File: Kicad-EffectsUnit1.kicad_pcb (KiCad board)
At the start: 2 copper layers, 100 x 100 mm, 167 parts, among them J101 In7, J102 Doepfer connector, J103 Vin 7-12v, J104 In6, J105 In3, J106 Out10, J107 Out11, J108 Out12, J109 Out13, J110 Power Conn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

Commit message: 3D + PCB
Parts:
- removed REF**: Gauge_100mm_Grid_Type1_Silk_CopperTop, AJ:Gauge_100mm_Grid_Type1_Silk_CopperTop
- removed SW103: Rotary_Encoder_Switch, Rotary_Encoder:RotaryEncoder_Alps_EC11E-Switch_Vertical_H20mm
- added C118: 100n, Capacitor_SMD:C_0805_2012Metric_Pad1.15x1.40mm_HandSolder, F.Cu at (57.9, 101.3)
- added C121: 100n, Capacitor_SMD:C_0805_2012Metric_Pad1.15x1.40mm_HandSolder, F.Cu at (61.6, 101.3)
- added RV104: 10k_A4, Potentiometer_THT:Potentiometer_China_RK09_Single_Vertical_AJ, F.Cu at (102.5, 126.5)
- added RV105: 10k_A5, Potentiometer_THT:Potentiometer_China_RK09_Single_Vertical_AJ, F.Cu at (102.5, 114.0)
- added SW105: Dist 10, AJ-Dropbox-Kicad:SPDTx2, F.Cu at (110.0, 66.5)
- D103, D104, D105, D107, D109, D112, D118: moved to F.Cu
- D113: value LED_Out12 -> LED_Out6; moved to F.Cu
- D114: value LED_Out13 -> LED_Out9; moved to F.Cu
- J108: value Out12 -> Out9
- J109: value Out13 -> Out6
- RV101: value 10k_O10 -> 10k_O6
- RV103: value 100k_O12 -> 100k_O10
- SW101: value Dist 10 -> Dist 6
- SW102: value Crush A3 -> Crush A6
- SW104: value Dist 12 -> Rotary_Encoder_Switch; footprint AJ-Dropbox-Kicad:SPDTx2 -> Rotary_Encoder:RotaryEncoder_Alps_EC11E-Switch_Vertical_H20mm
- moved D109 116.5 mm to (90.9, 139.2)
- moved D112 103.7 mm to (91.8, 130.9)
- moved J101 100.0 mm to (130.0, 135.0), turned to 90 degrees
- moved D103 99.2 mm to (79.5, 130.5)
- moved RV102 93.0 mm to (137.5, 121.5), turned to 180 degrees
- moved D118 83.9 mm to (84.5, 101.0)
- moved D104 78.7 mm to (76.5, 117.0)
- moved D107 75.1 mm to (82.4, 122.7)
- moved J107 74.5 mm to (130.0, 111.5), turned to 90 degrees
- moved J102 74.0 mm to (119.0, 52.0)
- moved J110 72.2 mm to (97.0, 55.0)
- moved A101 67.4 mm to (73.0, 3.00)
- moved RV103 63.3 mm to (102.5, 82.5), turned to 0 degrees
- moved J104 62.2 mm to (130.0, 100.5), turned to 90 degrees
- moved RV101 55.3 mm to (137.5, 77.5), turned to 180 degrees
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- renumbered C118 to C119, C119 to C120, C120 to C122, C121 to C123
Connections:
- A101 pad 10: LED-Out11 -> LED-Out6
- A101 pad 11: LED-Out12 -> LED-Out9
- A101 pad 12: LED-Out13 -> Out9
- A101 pad 15: Out12 -> LED-Out10
- A101 pad 16: Out13 -> LED-Out11
- A101 pad 23: (no net) -> SDA-A4
- A101 pad 24: (no net) -> SCL-A5
- A101 pad 9: LED-Out10 -> Out6
- C122 pad 1: Out13Dist -> Out9Dist
- D110 pad 2: Out10Dist -> Out6Dist
- D111 pad 1: Out10Dist -> Out6Dist
- J108 pad T: Out12Dist -> Out9Dist
- J109 pad T: Out13Dist -> Out6Dist
- R115 pad 1: Out10Dist -> Out6Dist
- R118 pad 1: LED-Out12 -> LED-Out6
- R121 pad 1: LED-Out13 -> LED-Out9
- R124 pad 2: A6 -> A7
- R129 pad 1: Out12Dist -> Out10Dist
- R130 pad 1: Out12Dist -> Out10Dist
- R131 pad 2: Out12 -> Out10
- R133 pad 2: A7 -> A3
- R136 pad 1: Out13Dist -> Out9Dist
- R137 pad 1: Out13Dist -> Out9Dist
- R138 pad 2: Out13 -> Out9
- SW102 pad 1: Out10 -> Out6
- SW102 pad 3: A3 -> A6

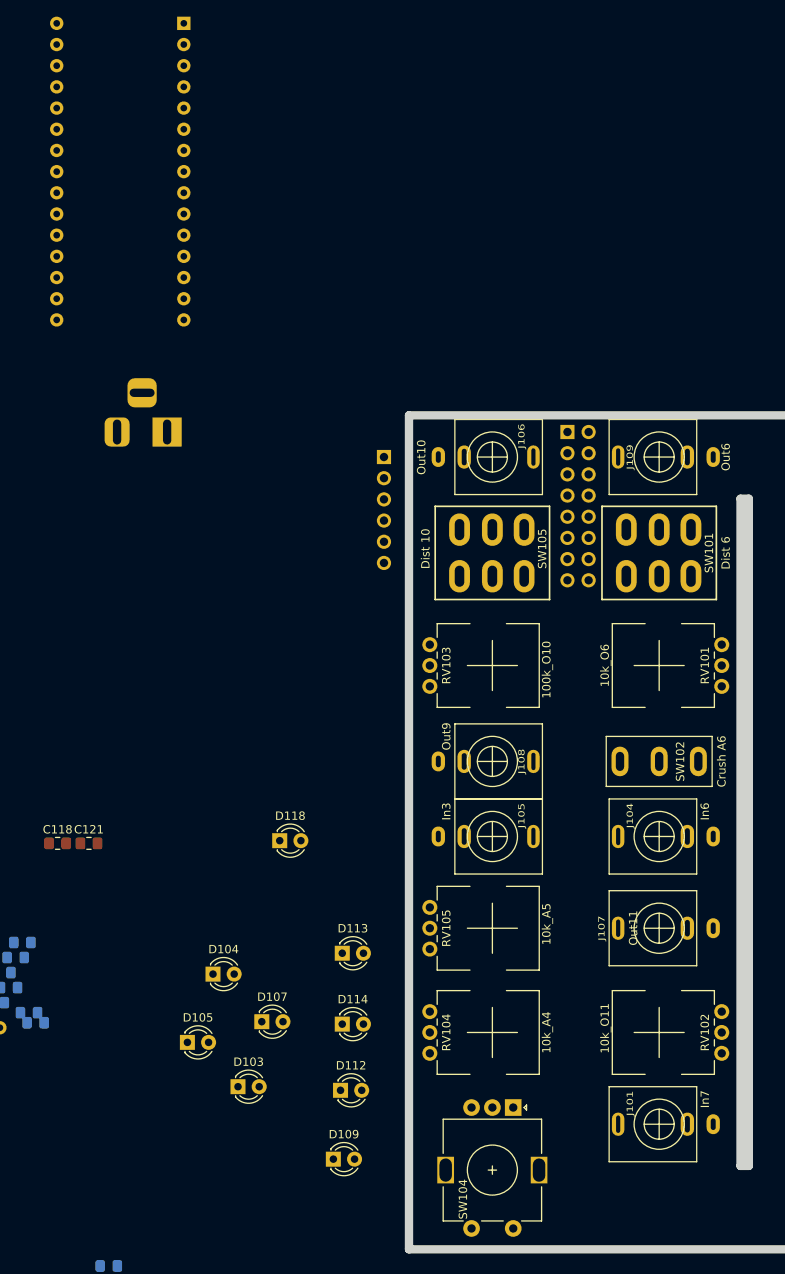
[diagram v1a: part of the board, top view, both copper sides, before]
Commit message: Removed components from PSU
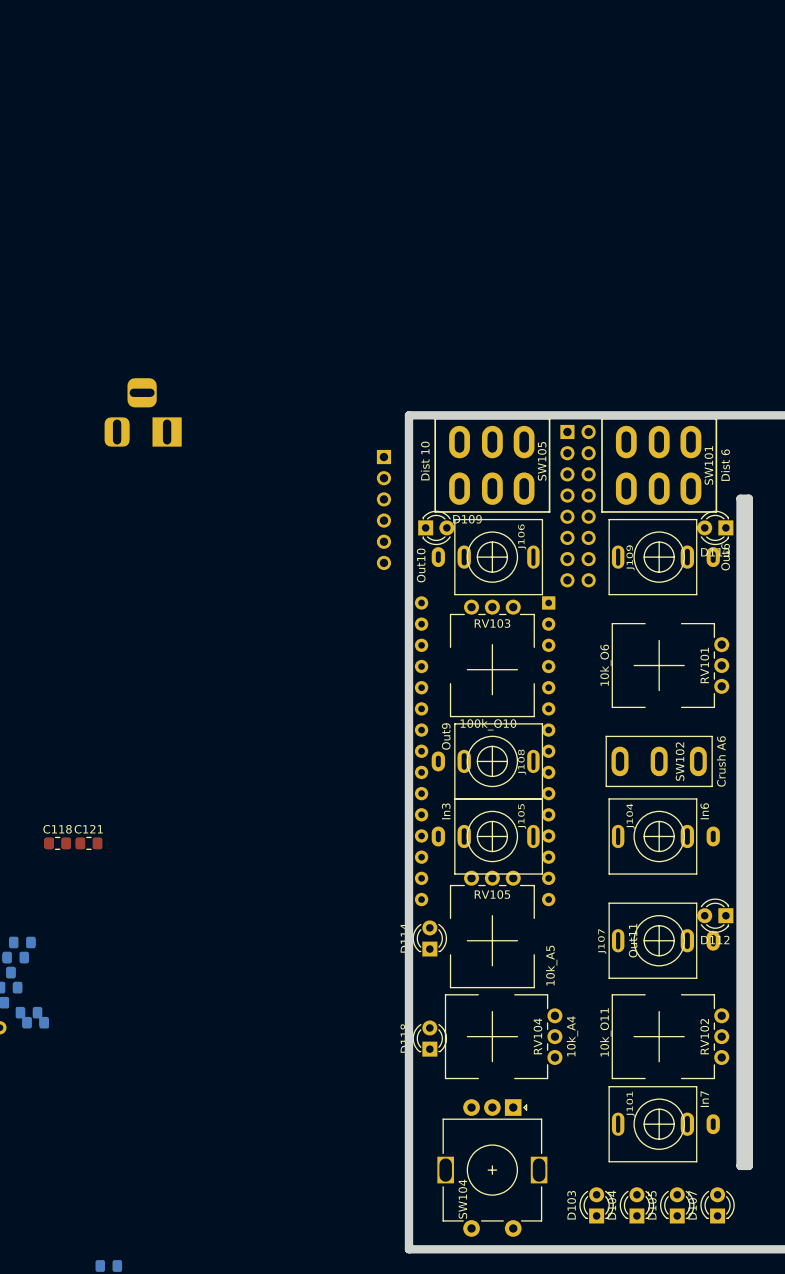
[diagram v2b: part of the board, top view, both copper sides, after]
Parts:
- moved A101 82.1 mm to (116.8, 72.5)
- moved D109 76.5 mm to (102.0, 63.5)
- moved D113 68.7 mm to (138.0, 63.5), turned to 180 degrees
- moved D105 62.3 mm to (132.2, 146.0), turned to 90 degrees
- moved D107 59.4 mm to (137.0, 146.0), turned to 90 degrees
- moved D104 58.5 mm to (127.3, 146.0), turned to 90 degrees
- moved D112 50.7 mm to (138.0, 110.0), turned to 180 degrees
- moved D103 45.7 mm to (122.5, 146.0), turned to 90 degrees
- moved D118 30.8 mm to (102.5, 126.0), turned to 90 degrees
- moved RV104 15.7 mm to (117.5, 122.0), turned to 180 degrees
- moved D114 13.8 mm to (102.5, 114.0), turned to 90 degrees
- moved J106 12.0 mm to (110.0, 67.0)
- moved J109 12.0 mm to (130.0, 67.0)
- moved RV103 10.7 mm to (107.5, 73.0), turned to 270 degrees
- moved SW101 10.5 mm to (130.0, 56.0)
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
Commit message: misc
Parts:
- removed C101: 100uF, Capacitor_THT:CP_Radial_D5.0mm_P2.50mm
- removed C102, C103: 100n, Capacitor_SMD:C_0805_2012Metric_Pad1.15x1.40mm_HandSolder
- removed F102: Polyfuse, Fuse:Fuse_1206_3216Metric_Pad1.42x1.75mm_HandSolder
- removed J103: Vin 7-12v, Connector_BarrelJack:BarrelJack_Horizontal
- removed J110: Power Conn, Connector_PinHeader_2.54mm:PinHeader_1x06_P2.54mm_Vertical
- removed R102: 10M, Resistor_SMD:R_0805_2012Metric_Pad1.15x1.40mm_HandSolder
- C118, C121: moved to B.Cu
- D110, D111: footprint Diode_SMD:D_SOD-123 -> Diode_SMD:D_0805_2012Metric_Pad1.15x1.40mm_HandSolder
- D117: value LED_Out11 -> LED_11dist
- D118: value LED_CV2 -> LED_11dist; footprint LED_THT:LED_D3.0mm -> Diode_SMD:D_0805_2012Metric_Pad1.15x1.40mm_HandSolder; moved to B.Cu
- moved F101 124.6 mm to (116.5, 57.0), turned to 270 degrees
- moved C106 116.9 mm to (128.0, 67.5), turned to 270 degrees
- moved C105 92.4 mm to (110.0, 63.5), turned to 180 degrees
- moved C110 85.4 mm to (113.0, 67.5), turned to 270 degrees
- moved C118 66.8 mm to (119.5, 127.0), turned to 270 degrees
- moved C119 53.0 mm to (86.8, 73.1)
- moved R114 53.0 mm to (74.8, 68.9)
- moved R125 53.0 mm to (68.4, 59.8)
- moved C107 53.0 mm to (56.5, 56.8)
- moved C108 53.0 mm to (54.9, 58.0)
- moved C109 53.0 mm to (57.3, 83.9)
- moved C111 53.0 mm to (54.1, 61.0)
- moved C112 53.0 mm to (53.3, 59.2)
- moved C123 53.0 mm to (76.4, 66.5)
- moved D101 53.0 mm to (62.9, 61.6)
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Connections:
- A101 pad 17: Net-(A101-Pad17) -> (no net)
- A101 pad 30: VCC -> (no net)
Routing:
- net +12V: track 0.00 -> 52.5 mm
- net -12V: track 0.00 -> 43.9 mm
- net +5V: track 0.00 -> 29.2 mm
- net GND: track 0.00 -> 7.62 mm
- net /+5Vin: track 0.00 -> 5.68 mm
- net /Gate: track 0.00 -> 2.54 mm
- net /CV: track 0.00 -> 2.54 mm

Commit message: PREPARE for major restruct
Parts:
- removed C109, C113: 100n, Capacitor_SMD:C_0805_2012Metric_Pad1.15x1.40mm_HandSolder
- moved R127 88.3 mm to (108.2, 145.8), turned to 180 degrees
- moved R122 83.7 mm to (129.0, 116.5), turned to 270 degrees
- moved C108 81.1 mm to (130.0, 88.8), turned to 180 degrees
- moved D117 78.6 mm to (127.0, 116.5), turned to 90 degrees
- moved R112 76.7 mm to (146.0, 82.0)
- moved U101 74.6 mm to (123.5, 86.2)
- moved D122 70.1 mm to (94.0, 47.2)
- moved C111 69.3 mm to (120.2, 81.8), turned to 180 degrees
- moved D116 64.7 mm to (122.0, 79.8), turned to 180 degrees
- moved C112 60.9 mm to (110.0, 81.5)
- moved D101 60.6 mm to (123.5, 62.8), turned to 270 degrees
- moved D121 60.5 mm to (94.0, 51.8)
- moved C107 59.1 mm to (111.0, 79.5), turned to 180 degrees
- moved U102 53.6 mm to (110.0, 86.2)
- moved R125 52.3 mm to (104.5, 97.8), turned to 180 degrees
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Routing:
- net +5V: track 29.2 -> 83.2 mm
- net GND: track 7.62 -> 37.6 mm
- net SCL-A5: track 0.00 -> 27.7 mm, vias 0 -> 1
- net +12V: track 52.5 -> 74.0 mm, vias 0 -> 2
- net Net-(SW102-Pad2): track 0.00 -> 19.6 mm
- net A3: track 0.00 -> 14.3 mm, vias 0 -> 1
- net Net-(D106-Pad1): track 0.00 -> 8.01 mm
- net Out11Dist: track 0.00 -> 5.78 mm
- net Btn: track 0.00 -> 5.37 mm
- net A1: track 0.00 -> 2.03 mm
- net A2: track 0.00 -> 2.01 mm
- net -12V: track 43.9 -> 45.2 mm

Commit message: Reorganize #1
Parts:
- moved R124 80.1 mm to (124.7, 104.2), turned to 90 degrees
- moved C117 77.5 mm to (113.8, 62.2), turned to 180 degrees
- moved R104 73.3 mm to (125.2, 96.0), turned to 90 degrees
- moved R119 59.2 mm to (131.5, 32.2)
- moved R121 56.4 mm to (118.5, 104.5), turned to 180 degrees
- moved R132 52.1 mm to (114.8, 108.0)
- moved R111 50.7 mm to (130.0, 36.2)
- moved C108 39.9 mm to (90.2, 85.8)
- moved D108 37.1 mm to (133.8, 43.2)
- moved D116 37.1 mm to (126.8, 43.0)
- moved R131 35.2 mm to (118.5, 108.0)
- moved R134 31.3 mm to (103.5, 52.2), turned to 90 degrees
- moved U101 22.9 mm to (130.0, 108.2)
- moved C111 22.9 mm to (98.3, 75.2)
- moved C107 19.8 mm to (91.3, 77.8)
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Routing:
- net Net-(C117-Pad2): track 0.00 -> 60.8 mm
- net +5V: track 83.2 -> 37.9 mm
- net -12V: track 45.2 -> 78.1 mm
- net +12V: track 74.0 -> 103.2 mm, vias 2 -> 0
- net SCL-A5: track 27.7 -> 0.67 mm, vias 1 -> 0
- net Out10Dist: track 0.00 -> 26.0 mm
- net Net-(SW102-Pad2): track 19.6 -> 0.00 mm
- net GND: track 37.6 -> 19.4 mm
- net Net-(R134-Pad2): track 0.00 -> 11.8 mm
- net Net-(D106-Pad1): track 8.01 -> 0.00 mm
- net Net-(D121-Pad1): track 0.00 -> 6.57 mm
- net Net-(D119-Pad2): track 0.00 -> 6.48 mm
- net A3: track 14.3 -> 8.20 mm, vias 1 -> 0
- net Btn: track 5.37 -> 0.00 mm
- net Net-(C117-Pad1): track 0.00 -> 3.86 mm
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
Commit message: Distortion - Bitcrunch components placed
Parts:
- moved R113 101.8 mm to (136.0, 141.0)
- moved H102 97.2 mm to (169.0, 159.9)
- moved H101 97.2 mm to (169.8, 155.7)
- moved R130 91.6 mm to (109.6, 70.4), turned to 270 degrees
- moved R119 85.3 mm to (133.2, 117.5), turned to 270 degrees
- moved R117 84.8 mm to (138.0, 60.2), turned to 90 degrees
- moved H103 83.6 mm to (160.0, 137.6)
- moved D111 82.4 mm to (130.0, 69.2), turned to 90 degrees
- moved R120 81.3 mm to (137.5, 120.0), turned to 90 degrees
- moved D106 80.8 mm to (130.2, 62.2)
- moved D116 74.5 mm to (135.2, 117.0), turned to 270 degrees
- moved R110 74.5 mm to (131.0, 141.0)
- moved R115 73.3 mm to (133.0, 71.0)
- moved R118 72.0 mm to (133.0, 73.0)
- moved R137 69.8 mm to (109.8, 91.6)
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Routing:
- net A7: track 0.00 -> 108.9 mm
- net Net-(D106-Pad1): track 0.00 -> 90.0 mm
- net Net-(R115-Pad2): track 0.00 -> 66.8 mm, vias 0 -> 2
- net GND: track 19.4 -> 82.3 mm, vias 0 -> 1
- net Btn: track 0.00 -> 48.2 mm, vias 0 -> 3
- net SDA-A4: track 0.00 -> 42.0 mm
- net A2: track 0.00 -> 39.0 mm, vias 0 -> 3
- net A1: track 0.00 -> 37.0 mm, vias 0 -> 3
- net Net-(R130-Pad2): track 0.00 -> 31.7 mm, vias 0 -> 2
- net SCL-A5: track 0.67 -> 32.1 mm, vias 0 -> 2
- net Net-(R137-Pad2): track 0.00 -> 24.0 mm
- net Out6: track 0.00 -> 22.3 mm, vias 0 -> 2
- net Net-(RV103-Pad2): track 0.00 -> 21.2 mm
- net Out9Dist: track 0.00 -> 20.3 mm, vias 0 -> 4
- net Net-(D110-Pad1): track 0.00 -> 20.1 mm
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
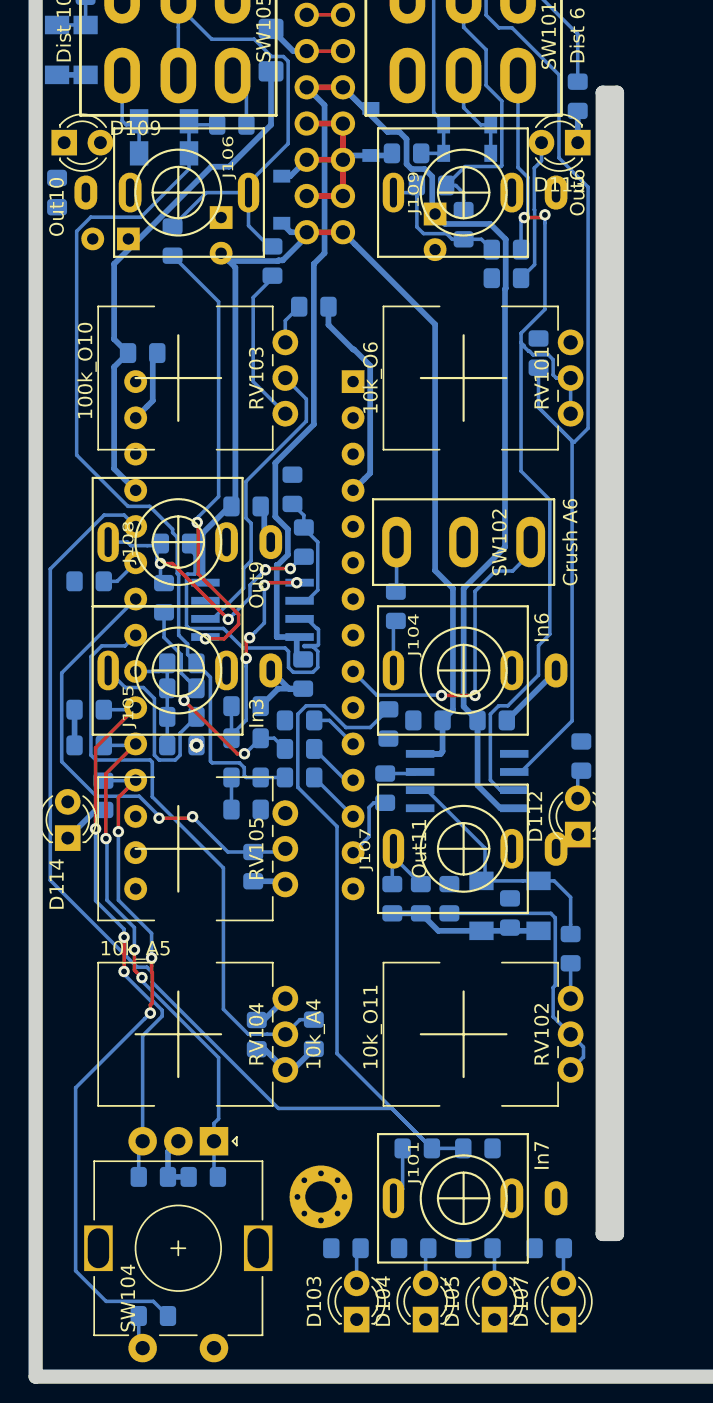
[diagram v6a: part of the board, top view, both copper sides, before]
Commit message: Before gnd flooding
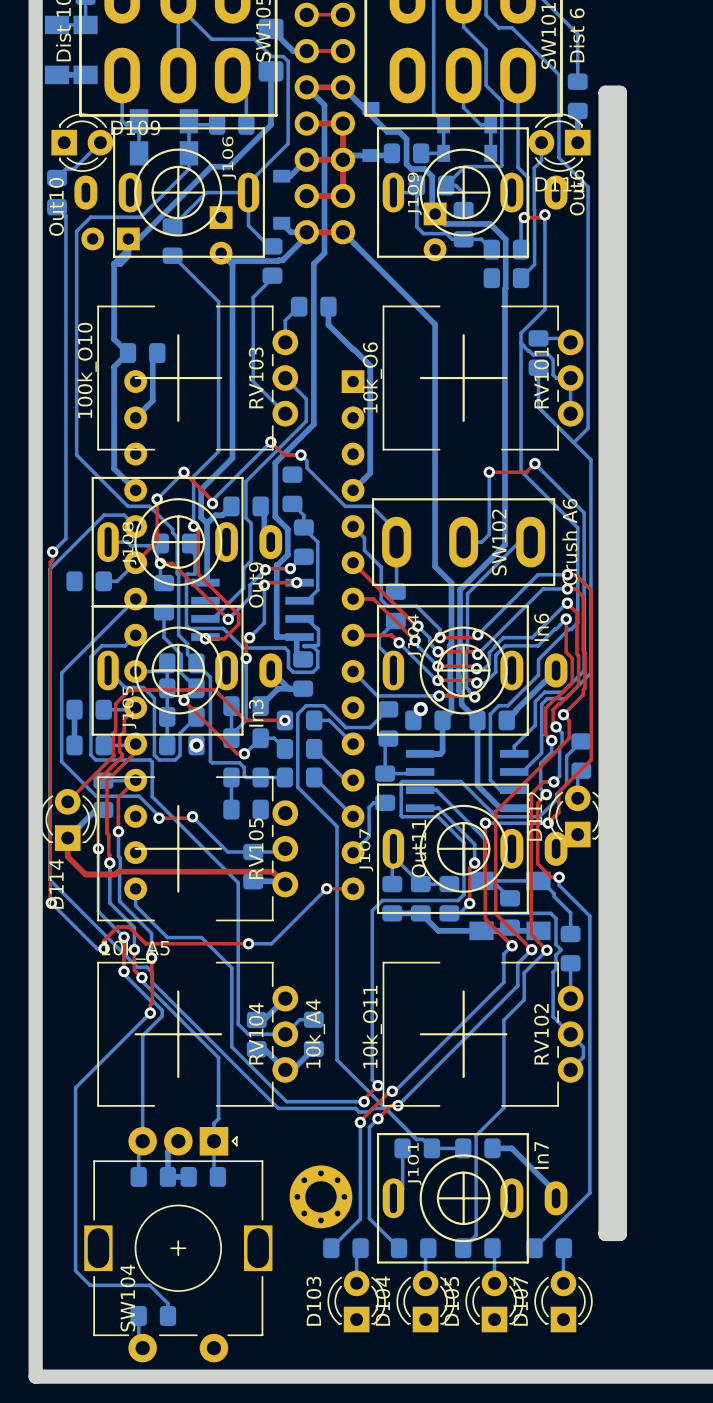
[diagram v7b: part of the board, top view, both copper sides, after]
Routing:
- net LED1: track 0.00 -> 82.4 mm, vias 0 -> 8
- net LED2: track 0.00 -> 76.7 mm, vias 0 -> 8
- net LED-Out11: track 0.00 -> 75.4 mm, vias 0 -> 2
- net LED-Out10: track 0.00 -> 75.1 mm, vias 0 -> 5
- net LED3: track 0.00 -> 70.3 mm, vias 0 -> 7
- net LED4: track 0.00 -> 68.3 mm, vias 0 -> 7
- net Net-(SW102-Pad2): track 0.00 -> 34.4 mm, vias 0 -> 2
- net A6: track 6.27 -> 35.5 mm, vias 0 -> 5
- net GND: track 82.3 -> 109.1 mm, vias 1 -> 2
- net Net-(D114-Pad2): track 0.00 -> 21.5 mm, vias 0 -> 1
- net Net-(R122-Pad2): track 19.5 -> 30.7 mm, vias 0 -> 2
- net Net-(D109-Pad2): track 0.00 -> 4.07 mm
- net Net-(R123-Pad1): track 2.25 -> 4.79 mm
- net +5V: track 41.2 -> 43.6 mm
- net -12V: track 81.1 -> 83.5 mm
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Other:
- outline, holes or cut-outs redrawn

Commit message: DRC done for Cruncher/Distortion
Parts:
- moved H102 6.93 mm to (162.2, 158.8)
- moved D114 0.45 mm to (102.7, 112.2)
- moved C110 0.25 mm to (113.0, 69.0)
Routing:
- net +5V: track 43.6 -> 103.5 mm, vias 0 -> 3
- net LED-Out6: track 0.00 -> 36.9 mm, vias 0 -> 3
- net GND: track 109.1 -> 135.6 mm, vias 2 -> 7
- net Net-(C120-Pad1): track 2.25 -> 24.2 mm, vias 0 -> 2
- net LED3: track 70.3 -> 67.1 mm, vias 7 -> 6
- net LED4: track 68.3 -> 65.3 mm
- net LED2: track 76.7 -> 74.4 mm
- net Out6: track 22.7 -> 20.9 mm
- net Net-(J104-PadT): track 4.37 -> 5.66 mm
- net -12V: track 83.5 -> 84.7 mm
- net LED1: track 82.4 -> 81.8 mm, vias 8 -> 9
- added copper zone on F.Cu, net GND
